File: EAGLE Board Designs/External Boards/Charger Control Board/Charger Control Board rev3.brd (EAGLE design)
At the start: 160 x 100 mm, 62 parts

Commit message: Made board file
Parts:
- removed CAN_TRANSCEIVER_3.1: MCP2551, HyTechDevices:SOIC-08
- added CAN_TRANSCEIVER_3.5: MCP2551, HyTechDevices:SOIC-08
- moved CAN_TRANSCEIVER_3.2 81.0 mm to (-38.1, 55.9)
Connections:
- net +5V: now also CAN_TRANSCEIVER_3.5.3; no longer CAN_TRANSCEIVER_3.1.3
- net CANH: now also CAN_TRANSCEIVER_3.5.7; no longer CAN_TRANSCEIVER_3.1.7
- net CANL: now also CAN_TRANSCEIVER_3.5.6; no longer CAN_TRANSCEIVER_3.1.6
- net GND: now also CAN_TRANSCEIVER_3.5.2, CAN_TRANSCEIVER_3.5.8; no longer CAN_TRANSCEIVER_3.1.2, CAN_TRANSCEIVER_3.1.8
- net N$15: now also CAN_TRANSCEIVER_3.2.4; no longer CAN_TRANSCEIVER_3.1.4
- net N$22: now also CAN_TRANSCEIVER_3.2.1; no longer CAN_TRANSCEIVER_3.1.1
- net N$4: now also CAN_TRANSCEIVER_3.5.4; no longer CAN_TRANSCEIVER_3.2.4
- net N$6: now also CAN_TRANSCEIVER_3.5.1; no longer CAN_TRANSCEIVER_3.2.1
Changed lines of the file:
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@@
 <attribute name="VALUE" x="-53.34" y="62.865" size="1.27" layer="27"/>
 </element>
-<element name="CAN_TRANSCEIVER_3.1" library="HyTechDevices" package="SOIC-08" value="MCP2551" x="-38.1" y="55.88" smashed="yes">
+<element name="CAN_TRANSCEIVER_3.2" library="HyTechDevices" package="SOIC-08" value="MCP2551" x="-38.1" y="55.88" smashed="yes">
 <attribute name="NAME" x="-40.64" y="55.88" size="0.6096" layer="25" rot="R90" align="bottom-center"/>
 <attribute name="VALUE" x="-35.56" y="55.88" size="0.6096" layer="27" rot="R270" align="bottom-center"/>
@@
 </element>
 <element name="U$5" library="HyTechDevices" package="TEENSY_3.5_EXT" value="TEENSY_3.5_EXT" x="-93.98" y="1.27" smashed="yes"/>
-<element name="CAN_TRANSCEIVER_3.2" library="HyTechDevices" package="SOIC-08" value="MCP2551" x="-91.44" y="-5.08" smashed="yes">
+<element name="CAN_TRANSCEIVER_3.5" library="HyTechDevices" package="SOIC-08" value="MCP2551" x="-91.44" y="-5.08" smashed="yes">
 <attribute name="NAME" x="-93.98" y="-5.08" size="0.6096" layer="25" rot="R90" align="bottom-center"/>
 <attribute name="VALUE" x="-88.9" y="-5.08" size="0.6096" layer="27" rot="R270" align="bottom-center"/>
@@
 <contactref element="C1" pad="1"/>
 <contactref element="C2" pad="1"/>
-<contactref element="CAN_TRANSCEIVER_3.1" pad="2"/>
+<contactref element="CAN_TRANSCEIVER_3.2" pad="2"/>
 <contactref element="U$4" pad="GND"/>
 <contactref element="STATUS" pad="C"/>
@@
 <contactref element="REG" pad="2"/>
 <contactref element="C3" pad="1"/>
-<contactref element="CAN_TRANSCEIVER_3.1" pad="8"/>
+<contactref element="CAN_TRANSCEIVER_3.2" pad="8"/>
 <contactref element="POWER" pad="P$1"/>
 <contactref element="MAIN" pad="P$3"/>
 <contactref element="D3" pad="A"/>
 <contactref element="U$3" pad="C2"/>
-<contactref element="CAN_TRANSCEIVER_3.2" pad="8"/>
-<contactref element="CAN_TRANSCEIVER_3.2" pad="2"/>
+<contactref element="CAN_TRANSCEIVER_3.5" pad="8"/>
+<contactref element="CAN_TRANSCEIVER_3.5" pad="2"/>
 <contactref element="C6" pad="1"/>
 <contactref element="C7" pad="1"/>
@@
 <contactref element="CAN_TERM_JMP" pad="1"/>
 <contactref element="U$1" pad="2"/>
-<contactref element="CAN_TRANSCEIVER_3.1" pad="7"/>
+<contactref element="CAN_TRANSCEIVER_3.2" pad="7"/>
 <contactref element="MAIN" pad="P$1"/>
-<contactref element="CAN_TRANSCEIVER_3.2" pad="7"/>
+<contactref element="CAN_TRANSCEIVER_3.5" pad="7"/>
 <wire x1="-52.07" y1="66.04" x2="-92.075" y2="-2.48" width="0" layer="19" extent="1-1"/>
 <wire x1="-38.735" y1="58.48" x2="-52.07" y2="66.04" width="0" layer="19" extent="1-1"/>
@@
 </signal>
 <signal name="CANL">
-<contactref element="CAN_TRANSCEIVER_3.1" pad="6"/>
+<contactref element="CAN_TRANSCEIVER_3.2" pad="6"/>
 <contactref element="U$1" pad="1"/>
 <contactref element="R9" pad="1"/>
 <contactref element="MAIN" pad="P$2"/>
-<contactref element="CAN_TRANSCEIVER_3.2" pad="6"/>
+<contactref element="CAN_TRANSCEIVER_3.5" pad="6"/>
 <wire x1="-37.465" y1="58.48" x2="-90.805" y2="-2.48" width="0" layer="19" extent="1-1"/>
 <wire x1="-29.19" y1="55.88" x2="-37.465" y2="58.48" width="0" layer="19" extent="1-1"/>
@@
 </signal>
 <signal name="+5V">
-<contactref element="CAN_TRANSCEIVER_3.1" pad="3"/>
+<contactref element="CAN_TRANSCEIVER_3.2" pad="3"/>
 <contactref element="C2" pad="2"/>
 <contactref element="C1" pad="2"/>
@@
 <contactref element="R6" pad="1"/>
 <contactref element="R5" pad="1"/>
-<contactref element="CAN_TRANSCEIVER_3.2" pad="3"/>
+<contactref element="CAN_TRANSCEIVER_3.5" pad="3"/>
 <contactref element="C6" pad="2"/>
 <contactref element="C7" pad="2"/>
@@
 <signal name="N$15">
 <contactref element="U$4" pad="D4(CANRX)"/>
-<contactref element="CAN_TRANSCEIVER_3.1" pad="4"/>
+<contactref element="CAN_TRANSCEIVER_3.2" pad="4"/>
 <wire x1="-30.48" y1="22.86" x2="-36.195" y2="53.28" width="0" layer="19" extent="1-1"/>
 </signal>
 <signal name="N$22">
 <contactref element="U$4" pad="D3(CANTX)"/>
-<contactref element="CAN_TRANSCEIVER_3.1" pad="1"/>
+<contactref element="CAN_TRANSCEIVER_3.2" pad="1"/>
 <wire x1="-30.48" y1="25.4" x2="-40.005" y2="53.28" width="0" layer="19" extent="1-1"/>
 </signal>
@@
 </signal>
 <signal name="N$4">
-<contactref element="CAN_TRANSCEIVER_3.2" pad="4"/>
+<contactref element="CAN_TRANSCEIVER_3.5" pad="4"/>
 <contactref element="U$5" pad="D4(CANRX)"/>
 <wire x1="-92.71" y1="48.26" x2="-89.535" y2="-7.68" width="0" layer="19" extent="1-1"/>
 </signal>
 <signal name="N$6">
-<contactref element="CAN_TRANSCEIVER_3.2" pad="1"/>
+<contactref element="CAN_TRANSCEIVER_3.5" pad="1"/>
 <contactref element="U$5" pad="D3(CANTX)"/>
 <wire x1="-92.71" y1="50.8" x2="-93.345" y2="-7.68" width="0" layer="19" extent="1-1"/>

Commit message: Layout_Update
Initial board size: 3.45 inches by 3.9 inches
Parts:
- moved U$5 175.5 mm to (63.5, 78.7), turned to 90 degrees
- moved SHUTDOWN_BUTTON 158.6 mm to (81.3, 55.9), turned to 270 degrees
- moved CHARGER 149.9 mm to (81.3, 63.5), turned to 270 degrees
- moved 5ABOARDFUSE 139.5 mm to (71.1, 29.2), turned to 90 degrees
- moved LED6 132.1 mm to (71.1, 72.4)
- moved LED4 120.2 mm to (71.1, 87.6)
- moved LED3 115.1 mm to (71.1, 95.2)
- moved 5ASHUTDOWNFUSE 114.9 mm to (82.5, 29.2), turned to 90 degrees
- moved CAN_TERM_JMP 110.6 mm to (59.7, 71.1), turned to 90 degrees
- moved S1 106.9 mm to (47.0, 72.4)
- moved LED1 100.5 mm to (71.1, 80.0)
- moved POWERTAIL 94.8 mm to (71.1, 63.5), turned to 270 degrees
- moved U$3 94.1 mm to (30.5, 6.35)
- moved U$4 90.3 mm to (38.1, 58.4), turned to 90 degrees
- moved POWER 90.0 mm to (71.1, 55.9), turned to 270 degrees
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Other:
- board size 160 x 100 mm -> 87.6 x 99.1 mm
- board text added: "BMS_OK"
- board text added: "HS_OK"
- board text added: "LATCH"
- board text added: "PWR_5V"

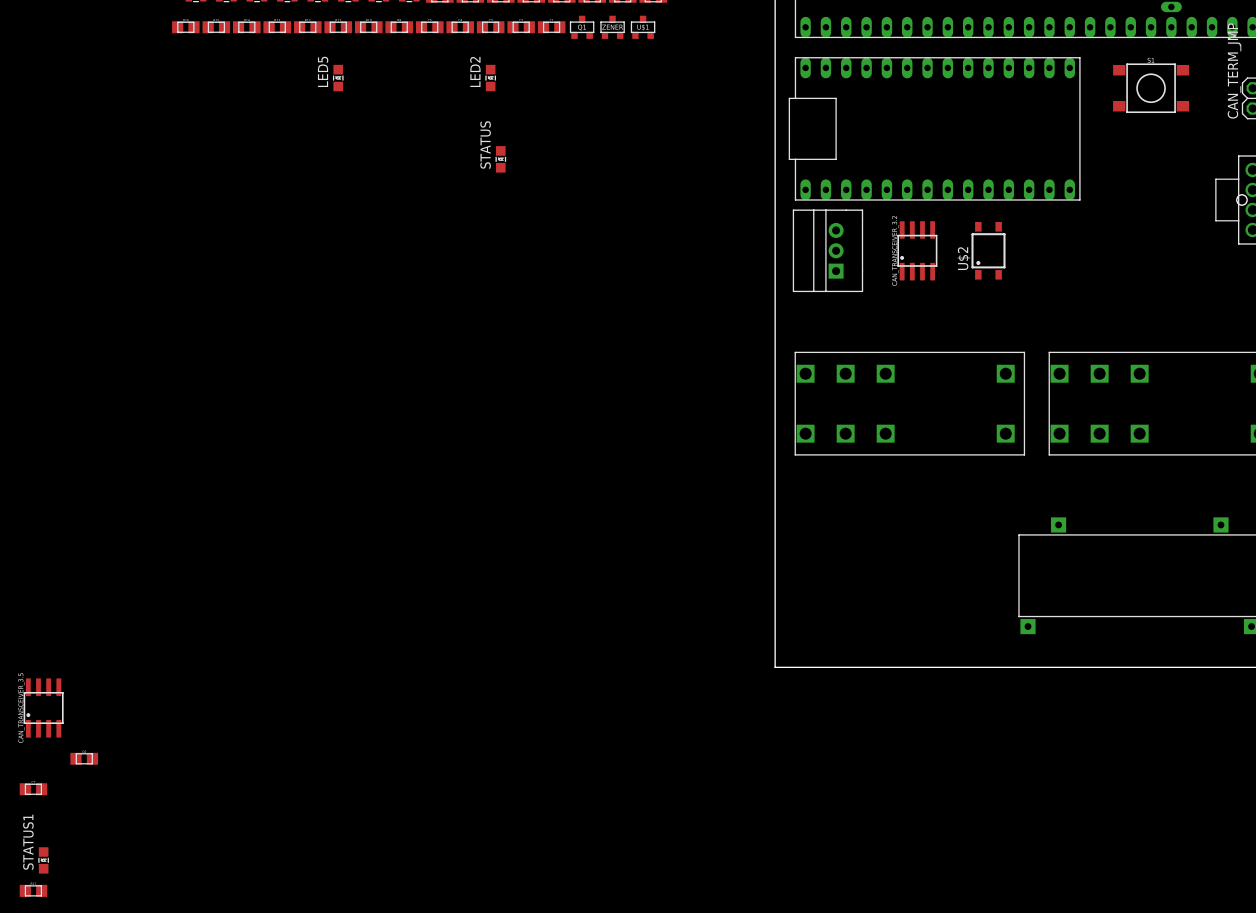
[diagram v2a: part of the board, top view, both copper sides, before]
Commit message: Layout_Update
3.45 * 3.9
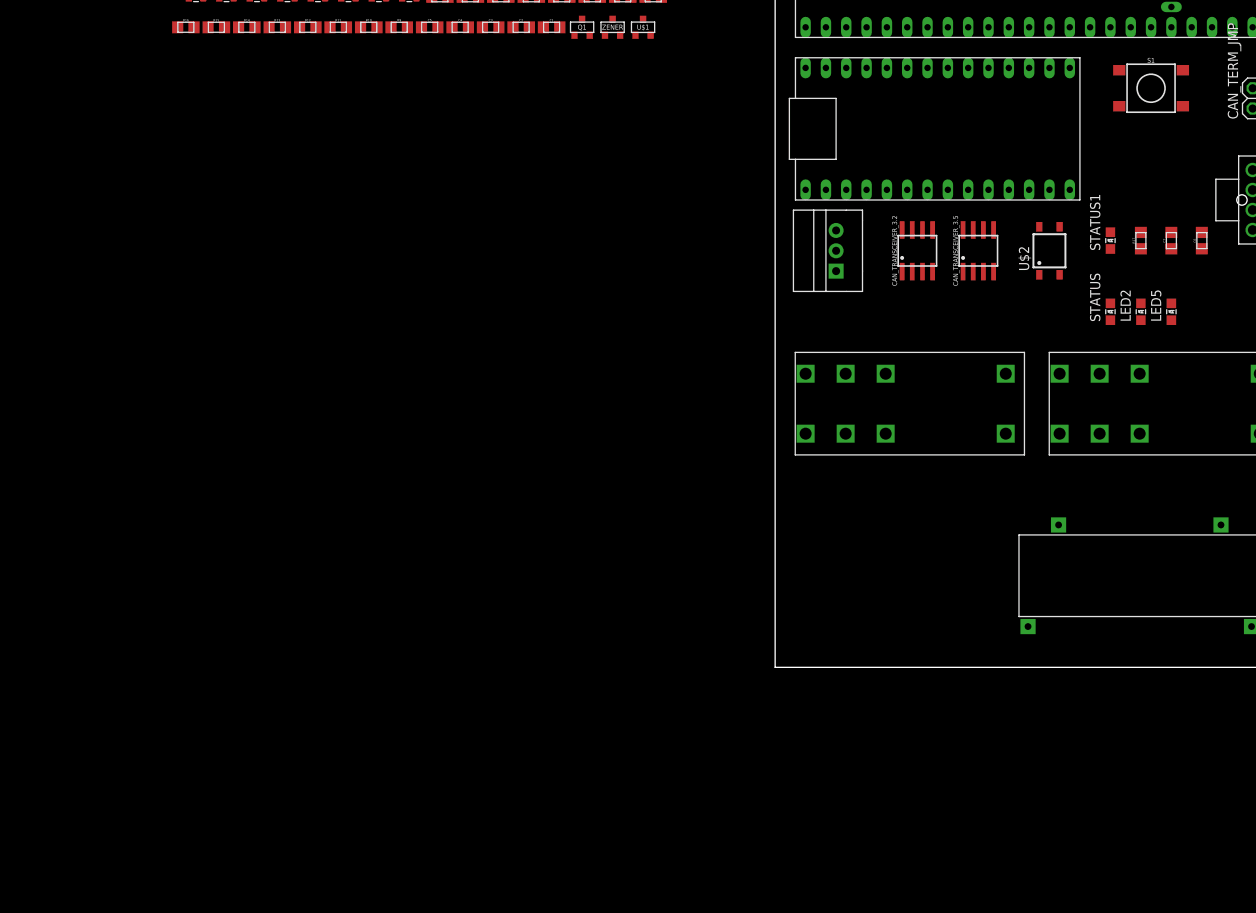
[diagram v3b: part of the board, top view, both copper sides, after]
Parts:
- moved R17 160.5 mm to (45.7, 53.3), turned to 90 degrees
- moved C7 157.9 mm to (49.5, 53.3), turned to 90 degrees
- moved STATUS1 154.2 mm to (41.9, 53.3)
- moved C6 154.0 mm to (53.3, 53.3), turned to 90 degrees
- moved CAN_TRANSCEIVER_3.5 130.1 mm to (25.4, 52.1)
- moved LED5 108.2 mm to (49.5, 44.5)
- moved LED2 86.4 mm to (45.7, 44.5)
- moved STATUS 78.5 mm to (41.9, 44.5)
- moved U$2 7.62 mm to (34.3, 52.1)

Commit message: Layout_Update
Layout outlook locked
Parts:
- moved R15 141.3 mm to (71.1, 69.8), turned to 90 degrees
- moved R14 136.0 mm to (67.3, 53.3), turned to 90 degrees
- moved D8 131.9 mm to (58.4, 48.3)
- moved R8 125.8 mm to (83.8, 86.4), turned to 270 degrees
- moved R7 122.3 mm to (83.8, 94.0), turned to 270 degrees
- moved R16 121.1 mm to (36.8, 30.5), turned to 270 degrees
- moved D5 120.2 mm to (58.4, 50.8)
- moved R6 119.1 mm to (83.8, 68.6), turned to 270 degrees
- moved D9 117.6 mm to (34.3, 34.3), turned to 90 degrees
- moved D4 115.8 mm to (58.4, 53.3)
- moved R5 114.5 mm to (83.8, 77.5), turned to 270 degrees
- moved D7 112.5 mm to (34.3, 30.5), turned to 90 degrees
- moved R12 112.2 mm to (49.5, 49.5), turned to 270 degrees
- moved D3 110.0 mm to (44.5, 26.7), turned to 180 degrees
- moved R13 109.1 mm to (36.8, 34.3), turned to 270 degrees
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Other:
- board size 87.6 x 99.1 mm -> 87.6 x 104.1 mm
- board text added: "GLV ~ 12V"
- board text added: "Tractive ~ 300V"

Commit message: Changed Board shape
Board shape
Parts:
- moved CHARGER 3.81 mm to (43.2, 11.4)
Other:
- board size 87.6 x 104.1 mm -> 87.6 x 99.1 mm

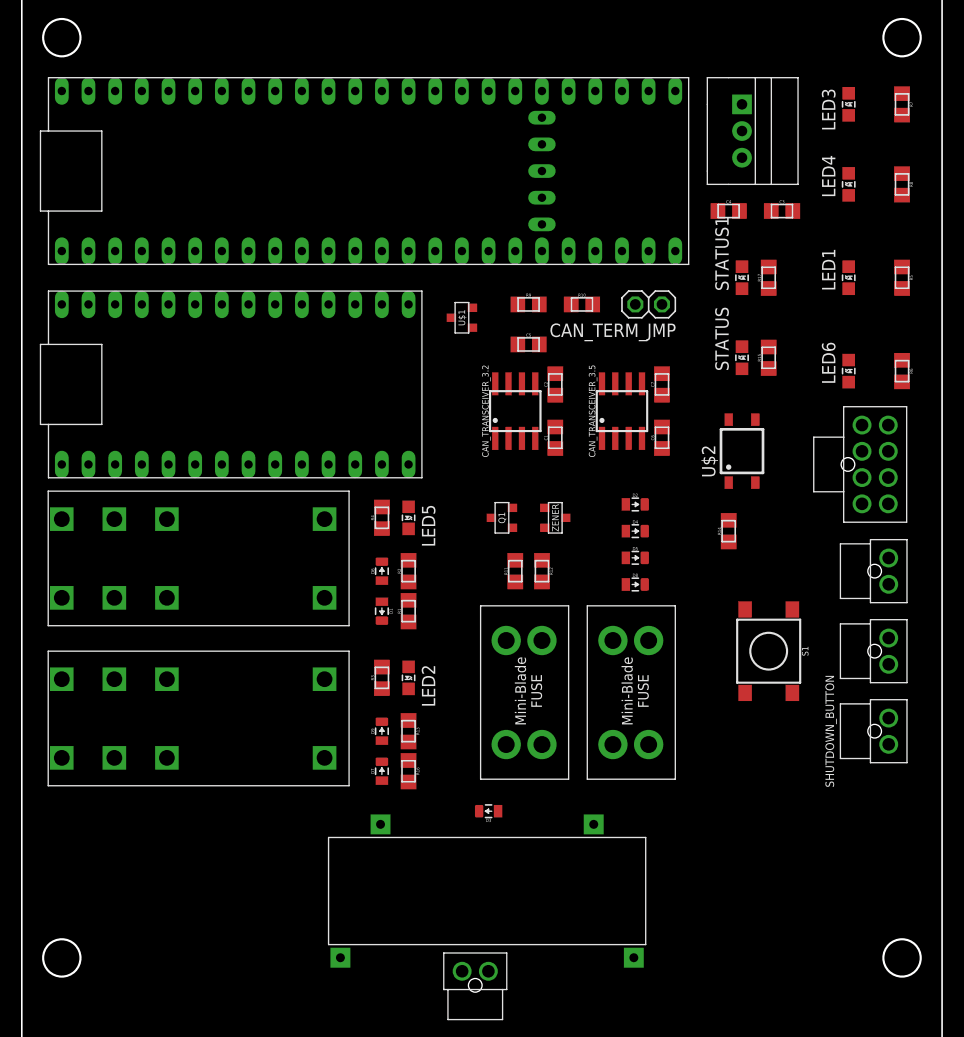
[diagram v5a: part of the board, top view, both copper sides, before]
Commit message: Increment Changes made to routing
- Pending issue: duplicate naming of BMS_OK signal in the schematic view, need schematic re-do and re-spin the layout because of the fact.
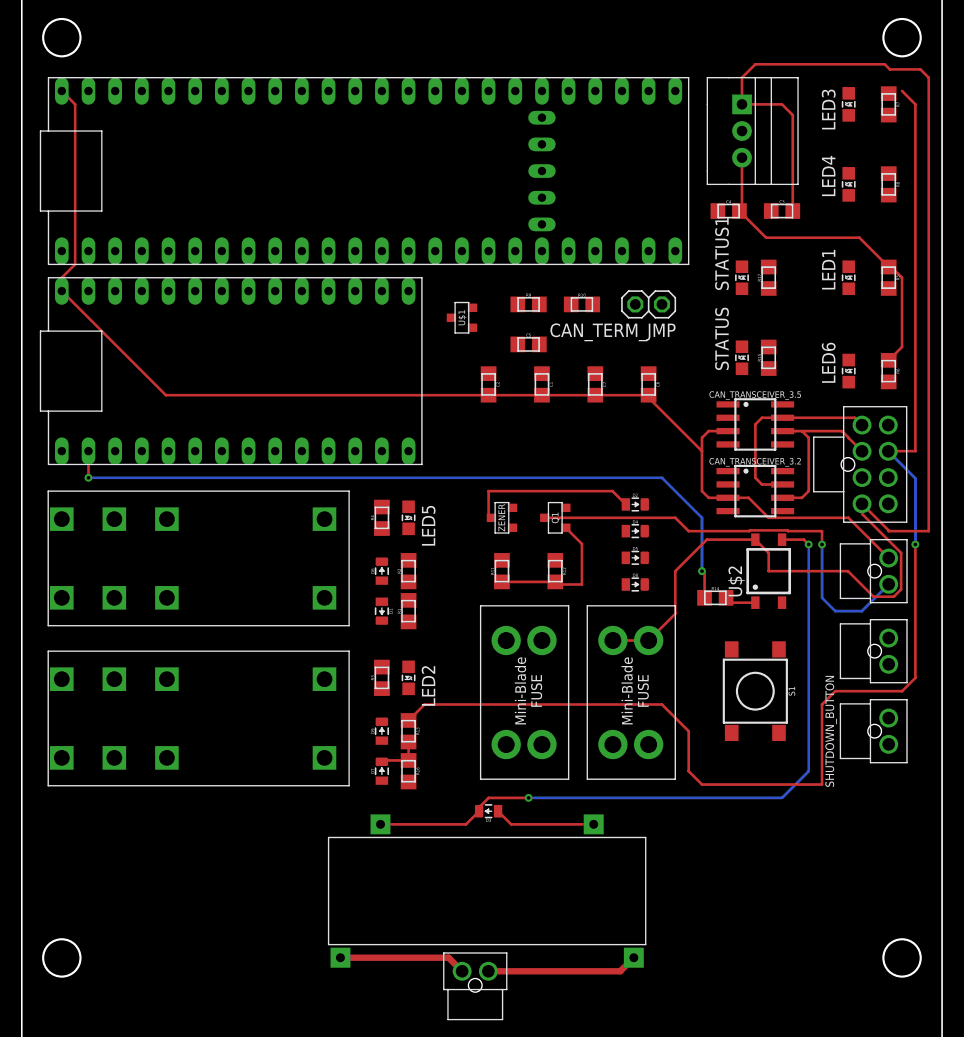
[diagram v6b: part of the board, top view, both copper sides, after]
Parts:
- moved CAN_TRANSCEIVER_3.2 24.1 mm to (69.8, 57.1), turned to 270 degrees
- moved CAN_TRANSCEIVER_3.5 12.8 mm to (69.8, 63.5), turned to 270 degrees
- moved U$2 11.7 mm to (71.1, 49.5)
- moved 5ABOARDFUSE 10.2 mm to (59.7, 33.0)
- moved 5ASHUTDOWNFUSE 10.2 mm to (49.5, 33.0)
- moved R14 6.48 mm to (66.0, 47.0), turned to 0 degrees
- moved C7 6.35 mm to (54.6, 67.3), turned to 270 degrees
- moved C2 6.35 mm to (44.5, 67.3), turned to 270 degrees
- moved C6 5.24 mm to (59.7, 67.3), turned to 270 degrees
- moved C1 5.24 mm to (49.5, 67.3), turned to 270 degrees
- moved Q1 5.08 mm to (50.8, 54.6)
- moved ZENER 5.08 mm to (45.7, 54.6), turned to 90 degrees
- moved S1 4.02 mm to (69.8, 38.1)
- moved R11 1.27 mm to (45.7, 49.5)
- moved R12 1.27 mm to (50.8, 49.5)
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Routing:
- net +5V: track 0.00 -> 147.4 mm
- net +12V: track 0.00 -> 133.4 mm
- net OKHS: track 0.00 -> 127.3 mm, vias 0 -> 1
- net TOGGLE_CHARGER: track 0.00 -> 70.3 mm, vias 0 -> 2
- net CHARGE_CONTROL: track 0.00 -> 67.4 mm, vias 0 -> 2
- net N$1: track 0.00 -> 41.3 mm, vias 0 -> 1
- net CANH: track 0.00 -> 18.7 mm
- net SHUTDOWN_D: track 0.00 -> 17.1 mm
- net CANL: track 0.00 -> 17.1 mm
- net CHARGER_2: track 0.00 -> 14.4 mm
- net N$5: track 0.00 -> 13.8 mm
- net CHARGER_1: track 0.00 -> 12.0 mm
- net GND: track 0.00 -> 9.63 mm
- net N$10: track 0.00 -> 2.98 mm
